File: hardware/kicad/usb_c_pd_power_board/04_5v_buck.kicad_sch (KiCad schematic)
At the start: 0 parts

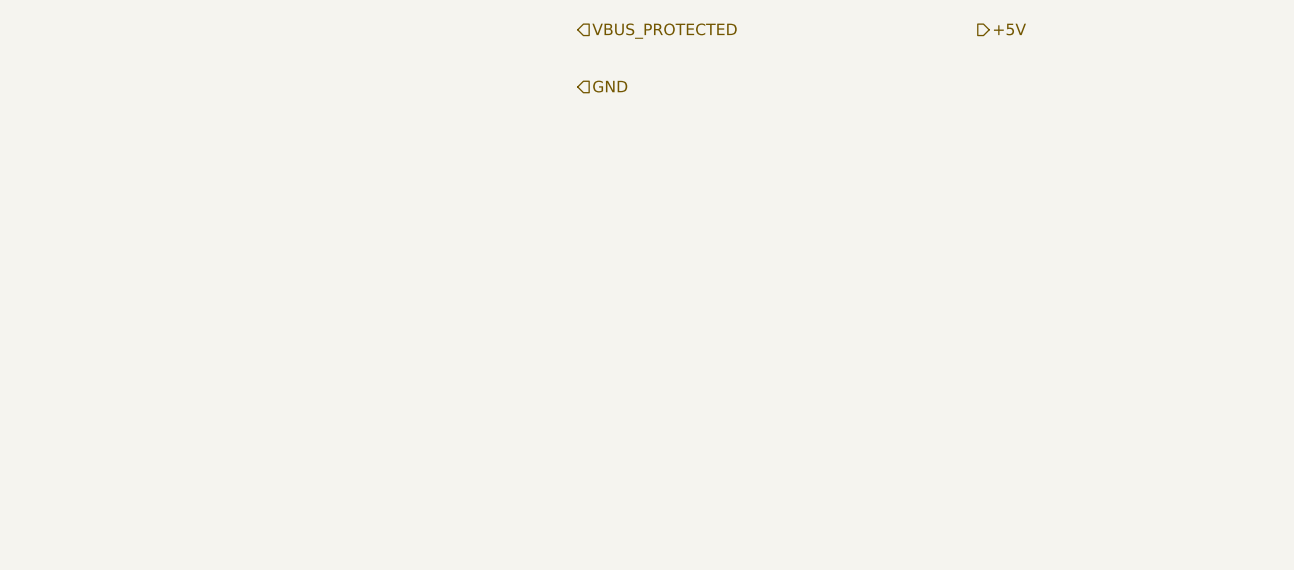
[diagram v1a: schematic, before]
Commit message: complete initial schematic and pass ERC
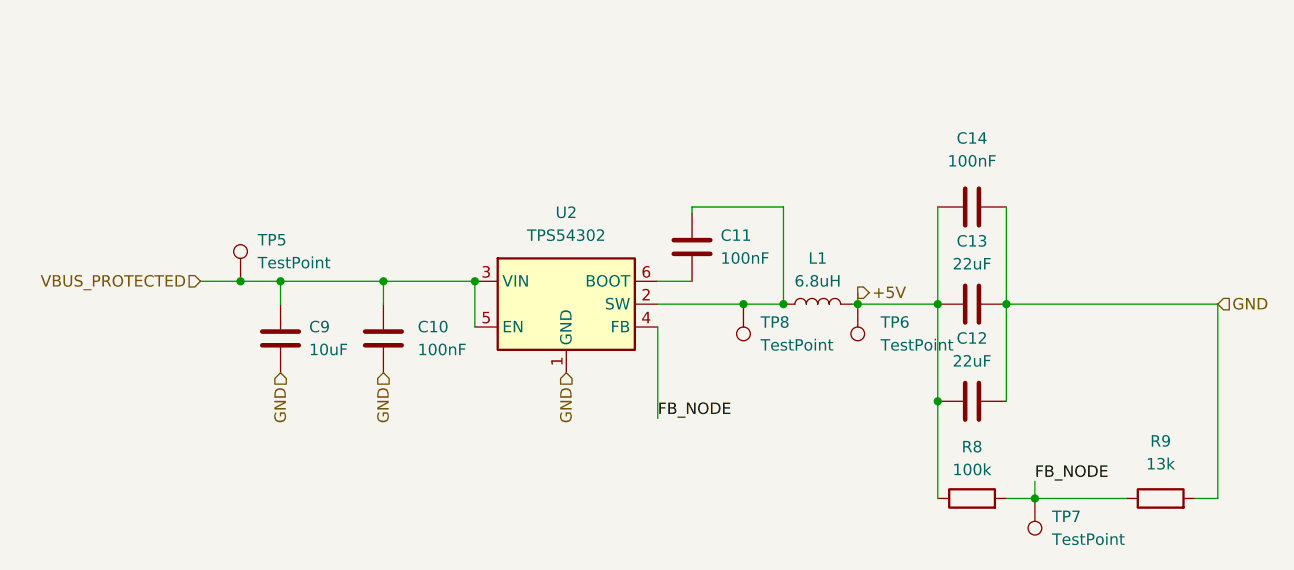
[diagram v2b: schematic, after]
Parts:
- added C10, C11, C14: 100nF, symbol Device:C
- added C12, C13: 22uF, symbol Device:C
- added C9: 10uF, symbol Device:C
- added L1: 6.8uH, symbol Device:L
- added R8: 100k, symbol Device:R
- added R9: 13k, symbol Device:R
- added TP5, TP6, TP7, TP8: TestPoint, symbol Connector:TestPoint
- added U2: TPS54302, Package_TO_SOT_SMD:SOT-23-6, symbol Regulator_Switching:TPS54302
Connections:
- net +5V: now also C12.1, C13.1, C14.1, L1.2, R8.1, TP6.1
- net GND: now also C10.2, C12.2, C13.2, C14.2, C9.2, R9.2, U2.1 (GND)
- net VBUS_PROTECTED: now also C10.1, C9.1, TP5.1, U2.3 (VIN), U2.5 (EN)
- new net: C11.2, L1.1, TP8.1, U2.2 (SW)
- new net: C11.1, U2.6 (BOOT)
- new net FB_NODE: R8.2, R9.1, TP7.1, U2.4 (FB)

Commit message: complete MVP: Schematic & PCB Design
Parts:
- C10, C11, C14: footprint (none) -> Capacitor_SMD:C_0603_1608Metric
- C12, C13, C9: footprint (none) -> Capacitor_SMD:C_0805_2012Metric
- L1: footprint (none) -> Inductor_SMD:L_Bourns-SRN6028
- R8, R9: footprint (none) -> Resistor_SMD:R_0603_1608Metric
- TP5, TP6, TP7, TP8: footprint (none) -> TestPoint:TestPoint_Pad_D1.0mm
- U2: footprint Package_TO_SOT_SMD:SOT-23-6 -> Package_TO_SOT_SMD:SOT-563
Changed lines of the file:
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@@
   (junction (at 189.865 111.76) (diameter 0) (color 0 0 0 0)
   )
+  (junction (at 101.6 109.22) (diameter 0) (color 0 0 0 0)
+  )
   (junction (at 173.355 111.76) (diameter 0) (color 0 0 0 0)
   )
@@
     (stroke (width 0) (type default))
   )
-  (wire (pts (xy 100.33 109.22) (xy 104.775 109.22))
+  (wire (pts (xy 100.33 109.22) (xy 101.6 109.22))
     (stroke (width 0) (type default))
   )
@@
   )
   (wire (pts (xy 173.355 110.49) (xy 173.355 111.76))
+    (stroke (width 0) (type default))
+  )
+  (wire (pts (xy 101.6 109.22) (xy 104.775 109.22))
     (stroke (width 0) (type default))
   )
@@
       (effects (font (size 1.27 1.27)))
     )
-    (property "Footprint" "" (at 189.865 99.9998 0)
+    (property "Footprint" "Capacitor_SMD:C_0603_1608Metric" (at 189.865 99.9998 0)
       (effects (font (size 1.27 1.27)) hide)
     )
@@
       (effects (font (size 1.27 1.27)) (justify left))
     )
-    (property "Footprint" "" (at 109.855 109.22 0)
+    (property "Footprint" "TestPoint:TestPoint_Pad_D1.0mm" (at 109.855 109.22 0)
       (effects (font (size 1.27 1.27)) hide)
     )
@@
       (effects (font (size 1.27 1.27)) (justify left))
     )
-    (property "Footprint" "" (at 110.1852 119.38 0)
+    (property "Footprint" "Capacitor_SMD:C_0805_2012Metric" (at 110.1852 119.38 0)
       (effects (font (size 1.27 1.27)) hide)
     )
@@
     )
   )
+  (symbol (lib_id "power:PWR_FLAG") (at 101.6 109.22 0) (unit 1)
+    (in_bom yes) (on_board yes) (dnp no) (fields_autoplaced)
+    (property "Reference" "#FLG01" (at 101.6 107.315 0)
+      (effects (font (size 1.27 1.27)) hide)
+    )
+    (property "Value" "PWR_FLAG" (at 101.6 104.14 0)
+      (effects (font (size 1.27 1.27)))
+    )
+    (property "Footprint" "" (at 101.6 109.22 0)
+      (effects (font (size 1.27 1.27)) hide)
+    )
+    (property "Datasheet" "~" (at 101.6 109.22 0)
+      (effects (font (size 1.27 1.27)) hide)
+    )
+    (pin "1")
+    (instances
+      (project "usb_c_pd_power_board"
+        (path "/f21e9372-3849-4e8f-9112-7a98c5af3538/76a6fdc6-acf7-4928-baf2-3861bbf4b49d"
+          (reference "#FLG01") (unit 1)
+        )
+      )
+    )
+  )
   (symbol (lib_id "Connector:TestPoint") (at 160.655 111.76 180) (unit 1)
     (in_bom yes) (on_board yes) (dnp no) (fields_autoplaced)
@@
       (effects (font (size 1.27 1.27)) (justify right))
     )
-    (property "Footprint" "" (at 155.575 111.76 0)
+    (property "Footprint" "TestPoint:TestPoint_Pad_D1.0mm" (at 155.575 111.76 0)
       (effects (font (size 1.27 1.27)) hide)
     )
@@
       (effects (font (size 1.27 1.27)) (justify right))
     )
-    (property "Footprint" "" (at 153.9748 101.6 0)
+    (property "Footprint" "Capacitor_SMD:C_0603_1608Metric" (at 153.9748 101.6 0)
       (effects (font (size 1.27 1.27)) hide)
     )
@@
       (effects (font (size 1.27 1.27)))
     )
-    (property "Footprint" "" (at 207.01 135.128 90)
+    (property "Footprint" "Resistor_SMD:R_0603_1608Metric" (at 207.01 135.128 90)
       (effects (font (size 1.27 1.27)) hide)
     )
@@
       (effects (font (size 1.27 1.27)) (justify left))
     )
-    (property "Footprint" "" (at 121.6152 119.38 0)
+    (property "Footprint" "Capacitor_SMD:C_0603_1608Metric" (at 121.6152 119.38 0)
       (effects (font (size 1.27 1.27)) hide)
     )
@@
       (effects (font (size 1.27 1.27)))
     )
-    (property "Footprint" "" (at 189.865 121.5898 0)
+    (property "Footprint" "Capacitor_SMD:C_0805_2012Metric" (at 189.865 121.5898 0)
       (effects (font (size 1.27 1.27)) hide)
     )
@@
       (effects (font (size 1.27 1.27)))
     )
-    (property "Footprint" "Package_TO_SOT_SMD:SOT-23-6" (at 142.24 120.65 0)
+    (property "Footprint" "Package_TO_SOT_SMD:SOT-563" (at 142.24 120.65 0)
       (effects (font (size 1.27 1.27)) (justify left) hide)
     )
@@
       (effects (font (size 1.27 1.27)))
     )
-    (property "Footprint" "" (at 186.055 135.128 90)
+    (property "Footprint" "Resistor_SMD:R_0603_1608Metric" (at 186.055 135.128 90)
       (effects (font (size 1.27 1.27)) hide)
     )
@@
       (effects (font (size 1.27 1.27)) (justify right))
     )
-    (property "Footprint" "" (at 187.96 133.35 0)
+    (property "Footprint" "TestPoint:TestPoint_Pad_D1.0mm" (at 187.96 133.35 0)
       (effects (font (size 1.27 1.27)) hide)
     )
@@
       (effects (font (size 1.27 1.27)))
     )
-    (property "Footprint" "" (at 189.865 110.7948 0)
+    (property "Footprint" "Capacitor_SMD:C_0805_2012Metric" (at 189.865 110.7948 0)
       (effects (font (size 1.27 1.27)) hide)
     )
@@
       (effects (font (size 1.27 1.27)))
     )
-    (property "Footprint" "" (at 168.91 111.76 0)
+    (property "Footprint" "Inductor_SMD:L_Bourns-SRN6028" (at 168.91 111.76 0)
       (effects (font (size 1.27 1.27)) hide)
     )
@@
       (effects (font (size 1.27 1.27)) (justify right))
     )
-    (property "Footprint" "" (at 168.275 111.76 0)
-      (effects (font (size 1.27 1.27)) hide)
-    )
+    (property "Footprint" "TestPoint:TestPoint_Pad_D1.0mm" (at 168.275 111.76 0)
+      (effects (font (size 1.27 1.27)) hide)
+    )
